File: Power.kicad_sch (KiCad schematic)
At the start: 5 parts, among them U1 UCC28881

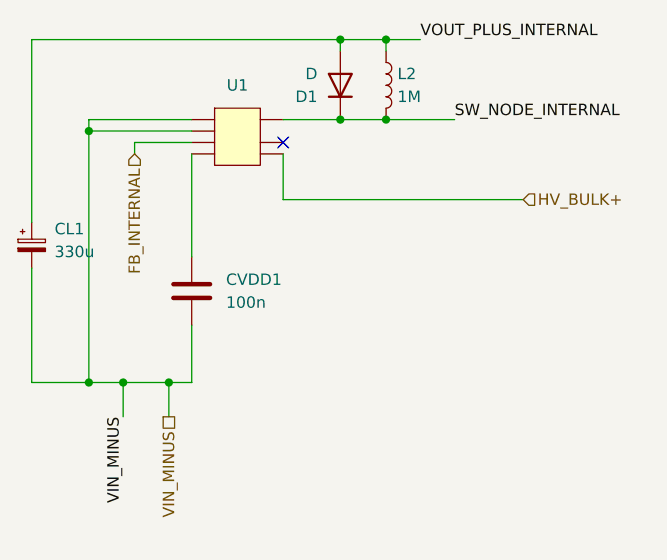
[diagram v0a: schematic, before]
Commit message: Updated schematic and fixed silkscreen overlap
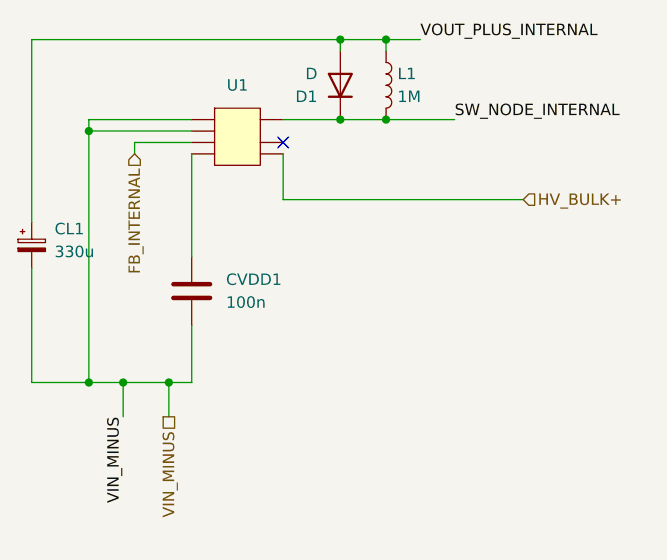
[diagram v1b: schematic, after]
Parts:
- renumbered L2 to L1
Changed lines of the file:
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@@
       (effects (font (size 1.27 1.27)) hide)
     )
-    (property "Datasheet" "https://www.digikey.com/en/products/detail/illinois-capacitor/337CKE035M/5412313?curr=usd" (at 66.04 92.71 0)
+    (property "Datasheet" "~" (at 66.04 92.71 0)
       (effects (font (size 1.27 1.27)) hide)
     )
@@
   (symbol (lib_id "Device:L") (at 105.41 74.93 0) (unit 1)
     (in_bom yes) (on_board yes) (dnp no) (fields_autoplaced)
-    (property "Reference" "L2" (at 106.68 73.66 0)
+    (property "Reference" "L1" (at 106.68 73.66 0)
       (effects (font (size 1.27 1.27)) (justify left))
     )
@@
       (effects (font (size 1.27 1.27)) hide)
     )
-    (property "Datasheet" "https://www.digikey.com/en/products/detail/eaton-electronics-division/DR127-102-R/953617?curr=usd" (at 105.41 74.93 0)
+    (property "Datasheet" "~" (at 105.41 74.93 0)
       (effects (font (size 1.27 1.27)) hide)
     )
@@
       (project "UC28881  WORK"
         (path "/02261b3b-0ab5-411c-b90d-2981c1ef32c1/50e508f9-c506-4c6b-8d20-c3808eadc697"
-          (reference "L2") (unit 1)
+          (reference "L1") (unit 1)
         )
       )
@@
       (effects (font (size 1.27 1.27)) hide)
     )
-    (property "Datasheet" "https://www.digikey.com/en/products/detail/taiyo-yuden/LMK105BJ104MV-F/2607802?curr=usd" (at 83.82 97.79 0)
+    (property "Datasheet" "~" (at 83.82 97.79 0)
       (effects (font (size 1.27 1.27)) hide)
     )
